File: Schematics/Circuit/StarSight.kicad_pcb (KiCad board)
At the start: 2 copper layers, 33 parts, among them IC1 LM2956-5V, J10 IR1, J11 IR1, J12 ultSound1, J13 ultSound1, J14 ultSound1, J15 ultSound1, J16 Conn_01x02, J17 Conn_01x02, J2 Line1, J3 Line2, J4 Line3, J5 Line4, J6 Line5, J7 IR1, J8 IR1, J9 IR1, P1 CONN_13X2, P2 Power, Q1 Q_NMOS_GDS, Q2 Q_NMOS_GDS

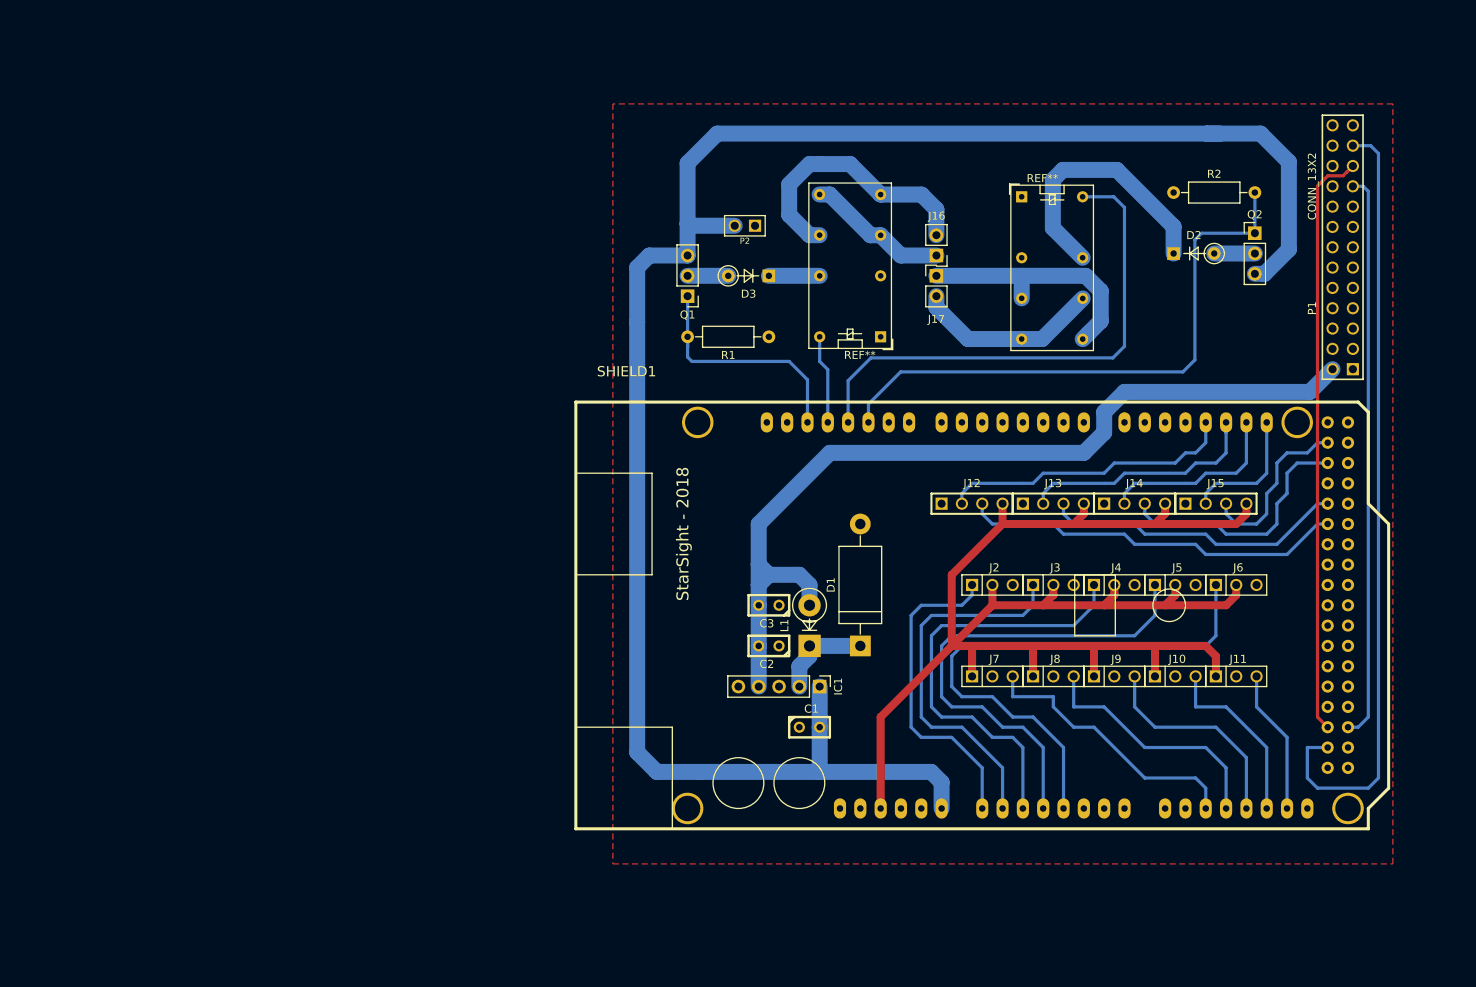
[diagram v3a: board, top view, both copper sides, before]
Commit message: Fix relays and board size
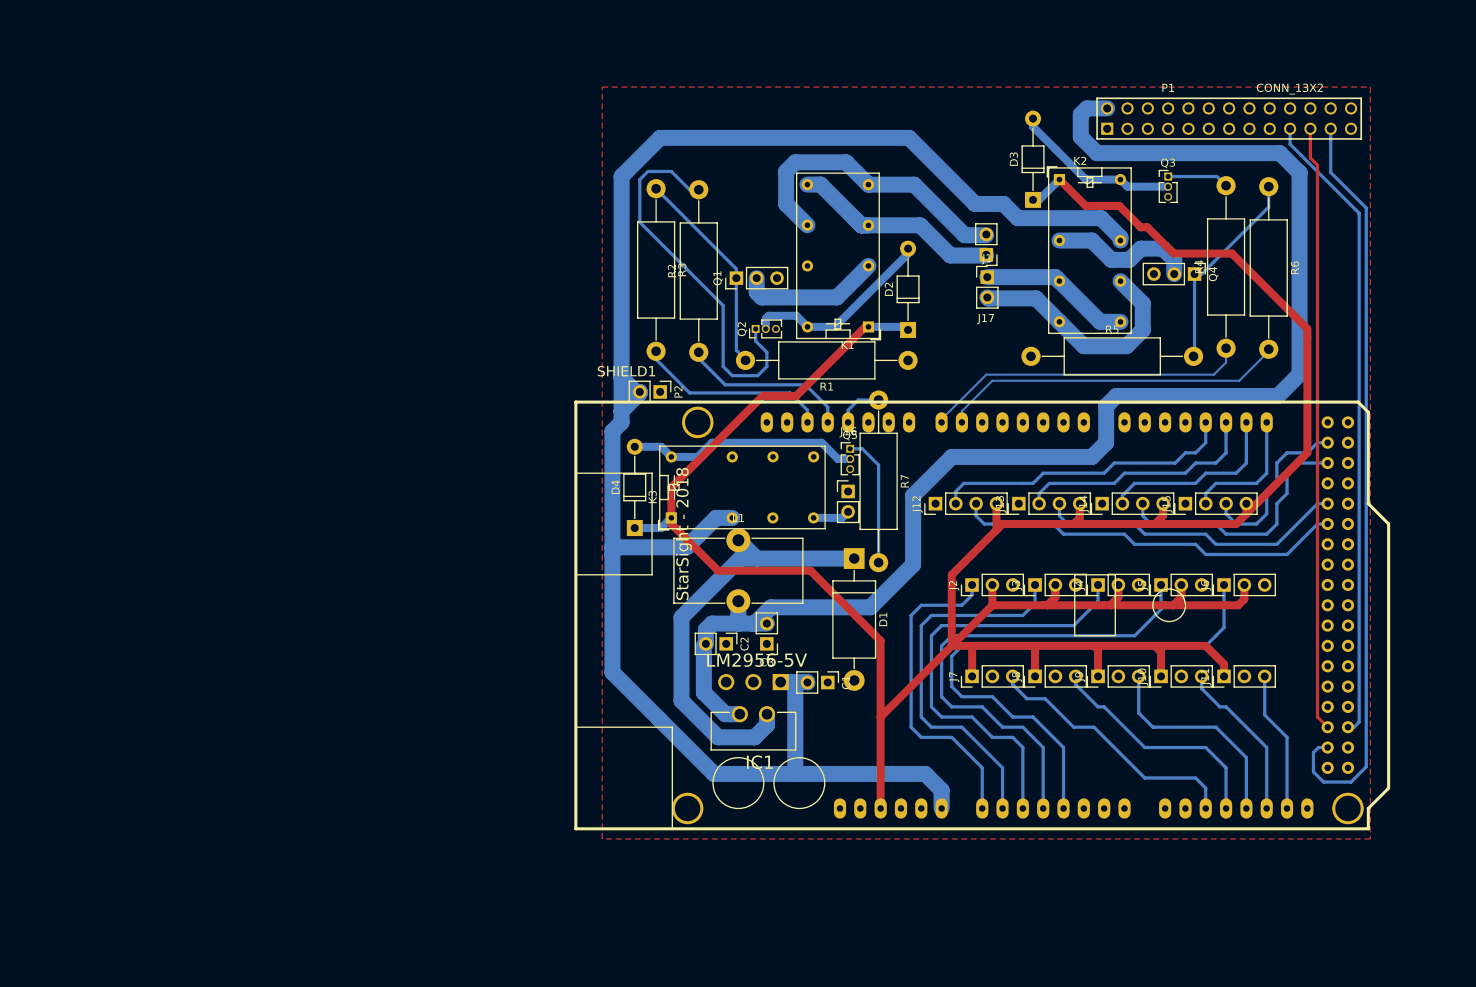
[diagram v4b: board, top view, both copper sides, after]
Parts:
- removed REF** (x2): Relay_DPDT_Omron_G5V-2, Relays_THT:Relay_DPDT_Omron_G5V-2
- added D4: 1N4007, Diodes_THT:D_T-1_P10.16mm_Horizontal, F.Cu at (110.2, 80.5)
- added J1: Conn_01x02, Pin_Headers:Pin_Header_Straight_1x02_Pitch2.54mm, F.Cu at (154.3, 49.1)
- added K1: RELAY, Relays_THT:Relay_DPDT_Omron_G5V-2, F.Cu at (139.4, 55.4)
- added K2: RELAY, Relays_THT:Relay_DPDT_Omron_G5V-2, F.Cu at (163.3, 37.0)
- added K3: RELAY, Relays_THT:Relay_DPDT_Omron_G5V-2, F.Cu at (114.8, 79.2)
- added Q3: Q_NPN_BCE, Pin_Headers:Pin_Header_Straight_1x03_Pitch1.27mm, F.Cu at (176.9, 36.6)
- added Q4: BUZZ TO220, Pin_Headers:Pin_Header_Straight_1x03_Pitch2.54mm, F.Cu at (180.2, 48.8)
- added Q5: Q_NPN_BCE, Pin_Headers:Pin_Header_Straight_1x03_Pitch1.27mm, F.Cu at (137.2, 70.6)
- added R3: 100, Resistors_THT:R_Axial_DIN0414_L11.9mm_D4.5mm_P20.32mm_Horizontal, F.Cu at (112.9, 38.1)
- added R4: 1k, Resistors_THT:R_Axial_DIN0414_L11.9mm_D4.5mm_P20.32mm_Horizontal, F.Cu at (184.2, 58.0)
- added R5: 10k, Resistors_THT:R_Axial_DIN0414_L11.9mm_D4.5mm_P20.32mm_Horizontal, F.Cu at (159.8, 59.1)
- added R6: 100, Resistors_THT:R_Axial_DIN0414_L11.9mm_D4.5mm_P20.32mm_Horizontal, F.Cu at (189.5, 37.8)
- added R7: 1k, Resistors_THT:R_Axial_DIN0414_L11.9mm_D4.5mm_P20.32mm_Horizontal, F.Cu at (140.7, 64.5)
- C1, C2, C3: footprint C1 -> Pin_Headers:Pin_Header_Straight_1x02_Pitch2.54mm
- D2, D3: value D -> 1N4007; footprint Diodes_THT:D_DO-35_SOD27_P5.08mm_Vertical_KathodeUp -> Diodes_THT:D_T-1_P10.16mm_Horizontal
- IC1: footprint Pin_Headers:Pin_Header_Straight_1x05_Pitch2.54mm -> reg:TO170P470X1016X2092-5P
- J10, J11, J2, J3, J4, J5, J6, J7, J8, J9: footprint PIN_ARRAY_3X1 -> Pin_Headers:Pin_Header_Straight_1x03_Pitch2.54mm
- J12, J13, J14, J15: footprint PIN_ARRAY_4x1 -> Pin_Headers:Pin_Header_Straight_1x04_Pitch2.54mm
- L1: footprint Diodes_THT:D_5W_P5.08mm_Vertical_KathodeUp -> Inductors_THT:L_Toroid_Vertical_L16.0mm_W8.0mm_P7.62mm
- P2: footprint PIN_ARRAY_2X1 -> Pin_Headers:Pin_Header_Straight_1x02_Pitch2.54mm
- Q1: value Q_NMOS_GDS -> BUZZ11 TO220
- Q2: value Q_NMOS_GDS -> Q_NPN_BCE; footprint Pin_Headers:Pin_Header_Straight_1x03_Pitch2.54mm -> Pin_Headers:Pin_Header_Straight_1x03_Pitch1.27mm
- R1: footprint Resistors_THT:R_Axial_DIN0207_L6.3mm_D2.5mm_P10.16mm_Horizontal -> Resistors_THT:R_Axial_DIN0414_L11.9mm_D4.5mm_P20.32mm_Horizontal
- R2: value 10k -> 1k; footprint Resistors_THT:R_Axial_DIN0207_L6.3mm_D2.5mm_P10.16mm_Horizontal -> Resistors_THT:R_Axial_DIN0414_L11.9mm_D4.5mm_P20.32mm_Horizontal
- SHIELD1: footprint ARDUINO_MEGA_SHIELD -> arduino_shields:ARDUINO_MEGA_SHIELD
- moved Q2 63.5 mm to (125.3, 55.6), turned to 90 degrees
- moved R2 62.6 mm to (118.2, 58.5), turned to 90 degrees
- moved D2 34.5 mm to (144.4, 55.8), turned to 90 degrees
- moved D3 34.4 mm to (160.0, 39.5), turned to 90 degrees
- moved J16 29.1 mm to (136.9, 75.9)
- moved P2 23.3 mm to (113.4, 63.5), turned to 270 degrees
- moved P1 21.5 mm to (184.5, 29.3), turned to 0 degrees
- moved R1 17.6 mm to (144.4, 59.6)
- moved IC1 16.5 mm to (121.7, 112.0), turned to 180 degrees
- moved L1 15.9 mm to (123.2, 82.0), turned to 0 degrees
- moved D1 10.9 mm to (137.7, 84.3), turned to 270 degrees
- moved Q1 6.50 mm to (122.9, 49.3), turned to 90 degrees
- moved J17 6.24 mm to (154.2, 46.4)
- moved C1 6.04 mm to (134.4, 99.8), turned to 270 degrees
- moved C2 5.34 mm to (121.7, 95.0), turned to 270 degrees
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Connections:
- D2 pad 1: Net-(D2-Pad1) -> +5V
- D3 pad 1: Net-(D3-Pad1) -> +5V
- J16 pad 1: Net-(J16-Pad1) -> GND
- P1 pad 1: Net-(P1-Pad1) -> (no net)
- P1 pad 10: /RXD -> (no net)
- P1 pad 11: /GPIO22 -> (no net)
- P1 pad 12: /GPIO18 -> (no net)
- P1 pad 13: Net-(P1-Pad13) -> (no net)
- P1 pad 14: Net-(P1-Pad14) -> (no net)
- P1 pad 15: Net-(P1-Pad15) -> (no net)
- P1 pad 16: /GPIO23 -> (no net)
- P1 pad 17: Net-(P1-Pad17) -> (no net)
- P1 pad 18: /GPIO24 -> (no net)
- P1 pad 20: Net-(P1-Pad20) -> (no net)
- P1 pad 22: /GPIO25 -> (no net)
- P1 pad 24: /GPIO8(CE0) -> (no net)
- P1 pad 25: Net-(P1-Pad25) -> (no net)
- P1 pad 26: /GPIO7(CE1) -> (no net)
- P1 pad 3: /GPIO0(SDA) -> (no net)
- P1 pad 4: Net-(P1-Pad4) -> (no net)
- P1 pad 5: /GPIO1(SCL) -> (no net)
- P1 pad 7: /GPIO17 -> (no net)
- P1 pad 8: /TXD -> (no net)
- P1 pad 9: Net-(P1-Pad9) -> (no net)
- Q1 pad 2: Net-(D3-Pad2) -> Net-(K1-Pad4)
- Q1 pad 3: +12V -> GND
- Q2 pad 3: +12V -> GND
- R2 pad 1: GND -> Net-(R2-Pad1)
- SHIELD1 pad 0: Net-(SHIELD1-Pad0) -> (no net)
- SHIELD1 pad 1: Net-(SHIELD1-Pad1) -> (no net)
- SHIELD1 pad 10: Net-(Q2-Pad1) -> (no net)
- SHIELD1 pad 12: Net-(K1-PadA2) -> Net-(R2-Pad1)
- SHIELD1 pad 14: Net-(SHIELD1-Pad14) -> (no net)
- SHIELD1 pad 15: Net-(SHIELD1-Pad15) -> (no net)
- SHIELD1 pad 16: Net-(SHIELD1-Pad16) -> (no net)
- SHIELD1 pad 17: Net-(SHIELD1-Pad17) -> (no net)
- SHIELD1 pad 2: Net-(SHIELD1-Pad2) -> (no net)
- SHIELD1 pad 23: Net-(SHIELD1-Pad23) -> (no net)
- SHIELD1 pad 25: Net-(SHIELD1-Pad25) -> (no net)
- SHIELD1 pad 26: Net-(SHIELD1-Pad26) -> (no net)
- SHIELD1 pad 27: Net-(SHIELD1-Pad27) -> (no net)
- SHIELD1 pad 29: Net-(SHIELD1-Pad29) -> (no net)
- SHIELD1 pad 3: Net-(SHIELD1-Pad3) -> (no net)
- SHIELD1 pad 31: Net-(SHIELD1-Pad31) -> (no net)
- SHIELD1 pad 32: Net-(SHIELD1-Pad32) -> (no net)
- SHIELD1 pad 33: Net-(SHIELD1-Pad33) -> (no net)
- SHIELD1 pad 34: Net-(SHIELD1-Pad34) -> (no net)
- SHIELD1 pad 35: Net-(SHIELD1-Pad35) -> (no net)
- SHIELD1 pad 36: Net-(SHIELD1-Pad36) -> (no net)
- SHIELD1 pad 37: Net-(SHIELD1-Pad37) -> (no net)
- SHIELD1 pad 38: Net-(SHIELD1-Pad38) -> (no net)
- SHIELD1 pad 39: Net-(SHIELD1-Pad39) -> (no net)
- SHIELD1 pad 3V3: Net-(SHIELD1-Pad3V3) -> (no net)
- SHIELD1 pad 4: Net-(SHIELD1-Pad4) -> (no net)
- SHIELD1 pad 40: Net-(SHIELD1-Pad40) -> (no net)
- SHIELD1 pad 41: Net-(SHIELD1-Pad41) -> (no net)
- SHIELD1 pad 42: Net-(SHIELD1-Pad42) -> (no net)
- SHIELD1 pad 43: Net-(SHIELD1-Pad43) -> (no net)
- SHIELD1 pad 44: Net-(SHIELD1-Pad44) -> (no net)
- SHIELD1 pad 45: Net-(SHIELD1-Pad45) -> (no net)
- SHIELD1 pad 46: Net-(SHIELD1-Pad46) -> (no net)
- SHIELD1 pad 47: Net-(SHIELD1-Pad47) -> (no net)
- SHIELD1 pad 48: Net-(SHIELD1-Pad48) -> (no net)
- SHIELD1 pad 49: Net-(SHIELD1-Pad49) -> (no net)
- SHIELD1 pad 5: Net-(SHIELD1-Pad5) -> (no net)
- SHIELD1 pad 53: Net-(SHIELD1-Pad53) -> (no net)
- SHIELD1 pad 5V_4: Net-(SHIELD1-Pad5V_4) -> (no net)
- SHIELD1 pad 5V_5: Net-(SHIELD1-Pad5V_5) -> (no net)
- SHIELD1 pad 8: Net-(SHIELD1-Pad8) -> (no net)
- SHIELD1 pad 9: Net-(SHIELD1-Pad9) -> (no net)
- SHIELD1 pad AD15: Net-(SHIELD1-PadAD15) -> (no net)
- SHIELD1 pad AD5: Net-(SHIELD1-PadAD5) -> (no net)
- SHIELD1 pad AD6: Net-(SHIELD1-PadAD6) -> (no net)
- SHIELD1 pad AD7: Net-(SHIELD1-PadAD7) -> (no net)
- SHIELD1 pad AD8: Net-(SHIELD1-PadAD8) -> (no net)
- SHIELD1 pad AD9: Net-(SHIELD1-PadAD9) -> (no net)
- SHIELD1 pad AREF: Net-(SHIELD1-PadAREF) -> (no net)
- SHIELD1 pad GND3: Net-(SHIELD1-PadGND3) -> (no net)
- SHIELD1 pad GND4: Net-(SHIELD1-PadGND4) -> (no net)
- SHIELD1 pad GND5: Net-(SHIELD1-PadGND5) -> (no net)
- SHIELD1 pad RST: Net-(SHIELD1-PadRST) -> (no net)
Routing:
- net +5V: track 185.3 -> 346.7 mm
- net Net-(C2-Pad2): track 113.3 -> 174.4 mm
- net Net-(R7-Pad1): track 64.7 -> 5.86 mm
- net Net-(R6-Pad2): track 0.00 -> 43.1 mm
- net Net-(D1-Pad1): track 12.0 -> 52.9 mm
- net Net-(R4-Pad1): track 0.00 -> 40.7 mm
- net Net-(D2-Pad1): track 33.2 -> 0.00 mm
- net Net-(J16-Pad1): track 31.1 -> 0.00 mm
- net Net-(J1-Pad2): track 0.00 -> 30.0 mm
- net Net-(D4-Pad2): track 0.00 -> 29.0 mm
- net Net-(Q4-Pad1): track 0.00 -> 25.6 mm
- net Net-(Q2-Pad1): track 73.3 -> 48.1 mm
- net Net-(R3-Pad2): track 0.00 -> 24.1 mm
- net Net-(R2-Pad1): track 0.00 -> 22.0 mm
- net Net-(J1-Pad1): track 0.00 -> 19.5 mm
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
